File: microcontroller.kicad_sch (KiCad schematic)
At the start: 11 parts, among them J1 TagConnect, U1 STM32H745XIH6

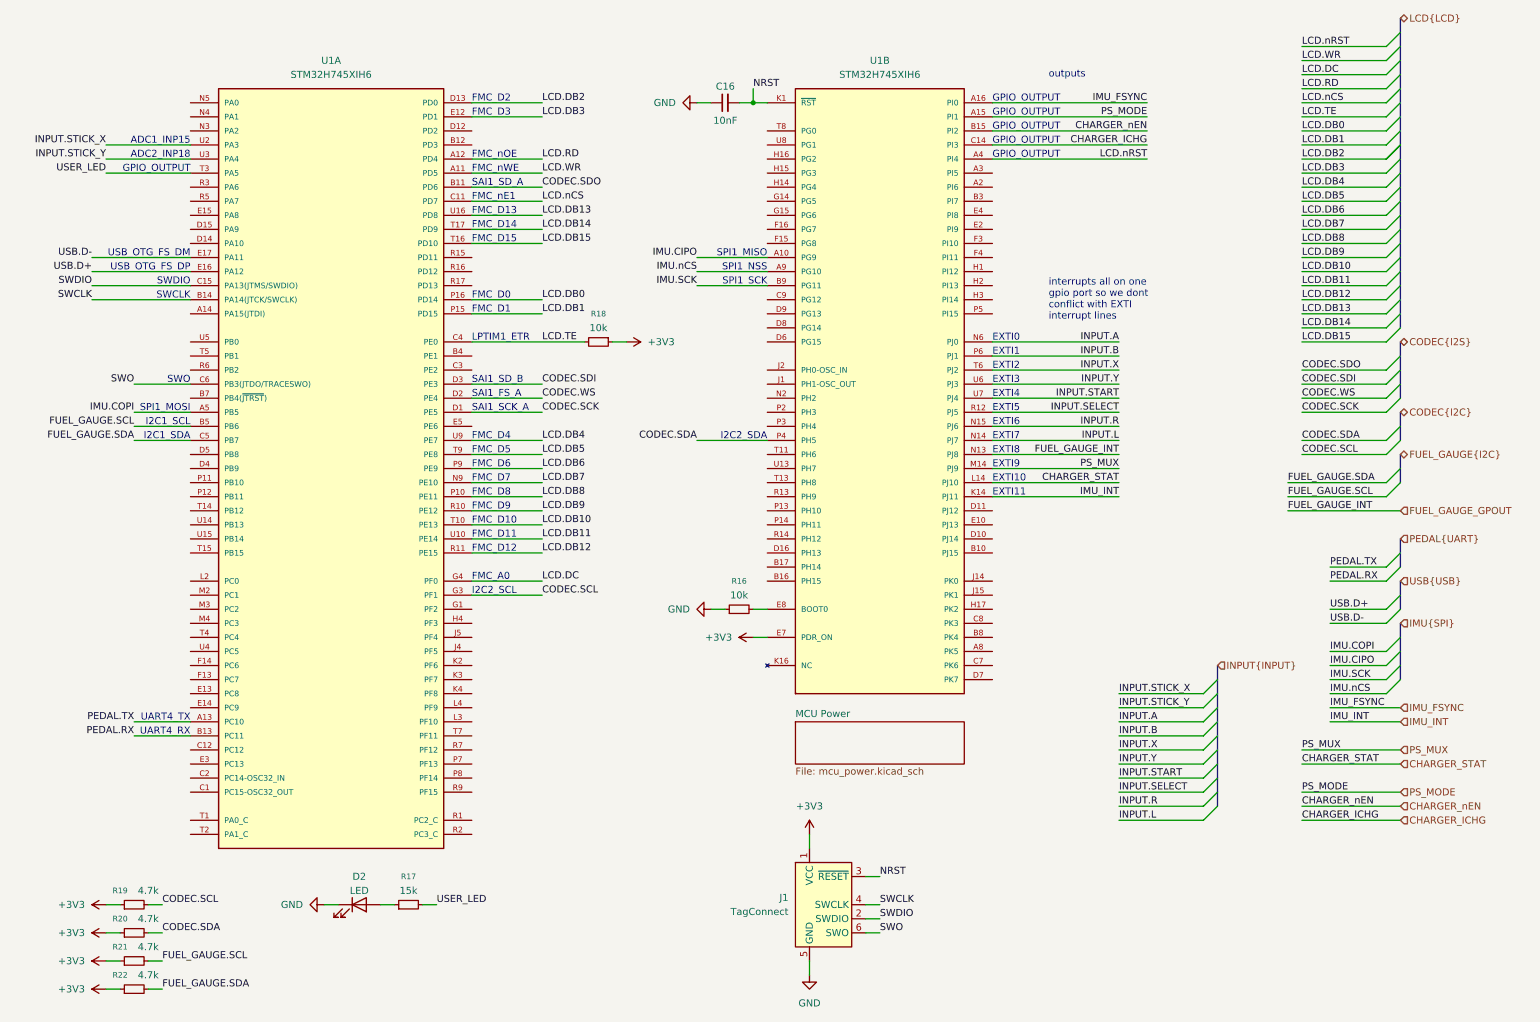
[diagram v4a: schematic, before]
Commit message: add no connects
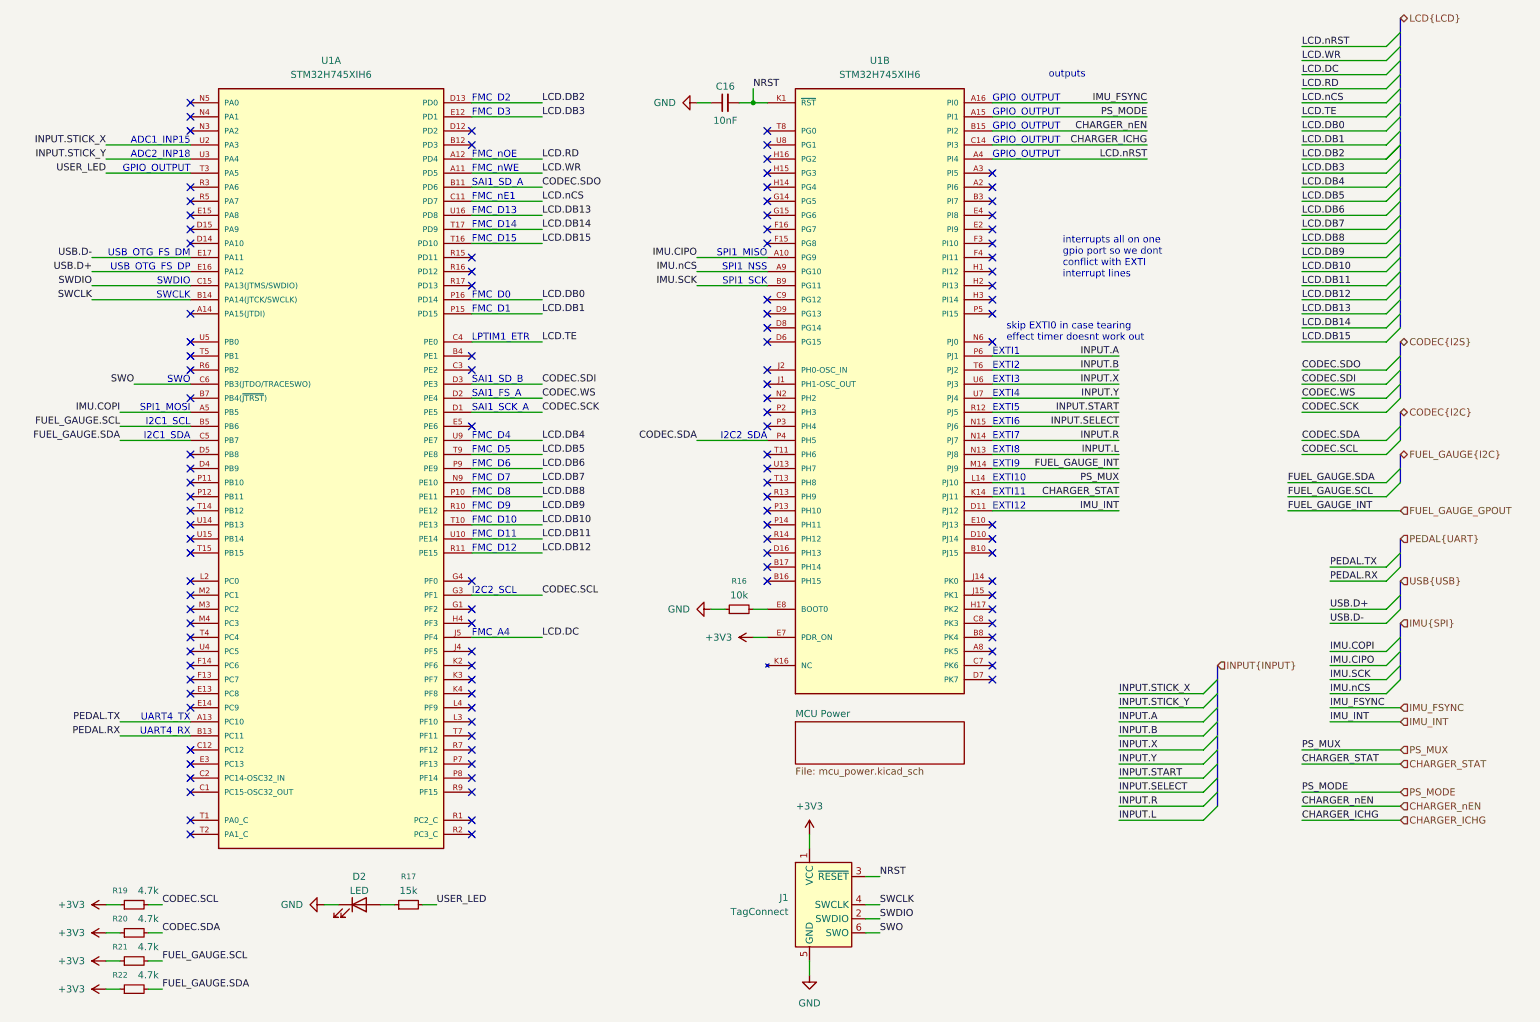
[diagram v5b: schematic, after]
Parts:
- removed R18: 10k, Resistor_SMD:R_0402_1005Metric, symbol Device:R_Small
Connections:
- net CHARGER_STAT: now also U1.K14 (PJ11); no longer U1.L14 (PJ10)
- net FUEL_GAUGE_GPOUT: now also U1.M14 (PJ9); no longer U1.N13 (PJ8)
- net IMU_INT: now also U1.D11 (PJ12); no longer U1.K14 (PJ11)
- net INPUT.A: now also U1.P6 (PJ1); no longer U1.N6 (PJ0)
- net INPUT.B: now also U1.T6 (PJ2); no longer U1.P6 (PJ1)
- net INPUT.L: now also U1.N13 (PJ8); no longer U1.N14 (PJ7)
- net INPUT.R: now also U1.N14 (PJ7); no longer U1.N15 (PJ6)
- net INPUT.SELECT: now also U1.N15 (PJ6); no longer U1.R12 (PJ5)
- net INPUT.START: now also U1.R12 (PJ5); no longer U1.U7 (PJ4)
- net INPUT.X: now also U1.U6 (PJ3); no longer U1.T6 (PJ2)
- net INPUT.Y: now also U1.U7 (PJ4); no longer U1.U6 (PJ3)
- net LCD.DC: now also U1.J5 (PF4); no longer U1.G4 (PF0)
- net PS_MUX: now also U1.L14 (PJ10); no longer U1.M14 (PJ9)
- no-connect marks 0 -> 112
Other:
- note added: "EXTI12"
- note added: "FMC_A4"
- note added: "skip EXTI0 in case tearing effect timer doesnt work out"
- note removed: "EXTI0"
- note removed: "FMC_A0"

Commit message: add oscillator
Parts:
- added C44: 1uF, Capacitor_SMD:C_0402_1005Metric, symbol Device:C_Small
- added U9: 8132H-25.000NL33DTL, custom:OSC-SMD_4P-L3.2-W2.5-BL, symbol custom:8132H-25.000NL33DTL
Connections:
- net +3V3: now also C44.1, U9.1 (E/D/NC), U9.4 (VCC)
- net GND: now also C44.2, U9.2 (GND)
- net 25MHz: now reaches U1.J2 (PH0-OSC_IN)
- net 25MHz: now also U9.3 (OUTPUT_RF)
- no-connect marks 112 -> 111
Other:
- moved on the sheet: D2, R17

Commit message: add imu sheet and library
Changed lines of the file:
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@@
 	)
 	(hierarchical_label "IMU{SPI}"
-		(shape input)
+		(shape bidirectional)
 		(at 261.62 127 0)
 		(effects
@@
 	)
 	(hierarchical_label "IMU_FSYNC"
-		(shape input)
+		(shape output)
 		(at 261.62 142.24 0)
 		(effects
